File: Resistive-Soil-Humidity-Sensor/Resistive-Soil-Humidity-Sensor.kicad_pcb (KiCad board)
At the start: 2 copper layers, 6 parts, among them Q1 BC547

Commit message: add pcb-layout
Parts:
- added H1: sensor, custom_libraryies:MountingHole.1.8mm, F.Cu at (231.8, 146.3)
- added H2: MountingHole_Pad, custom_libraryies:MountingHole.1.8mm, F.Cu at (231.8, 144.0)
- +9V1: moved to B.Cu
- moved Q1 134.5 mm to (218.8, 149.5)
- moved D1 131.4 mm to (209.7, 147.9), turned to 90 degrees
- moved R1 129.2 mm to (201.3, 144.1)
- moved Voltage-Reg1 127.5 mm to (193.7, 149.2)
- moved +9V1 127.3 mm to (187.1, 149.1)
- moved RV1 119.3 mm to (200.3, 147.6)
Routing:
- net Net-(BZ1-Pad1): track 0.00 -> 45.5 mm
- net Net-(+9V1-Pad2): track 0.00 -> 42.1 mm
- net Net-(H1-Pad1): track 0.00 -> 33.8 mm
- net Net-(BZ1-Pad2): track 0.00 -> 10.2 mm
- net Net-(D1-Pad2): track 0.00 -> 8.49 mm
- net Net-(+9V1-Pad1): track 0.00 -> 6.57 mm

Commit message: update footprints & recover design
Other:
- net class Default removed

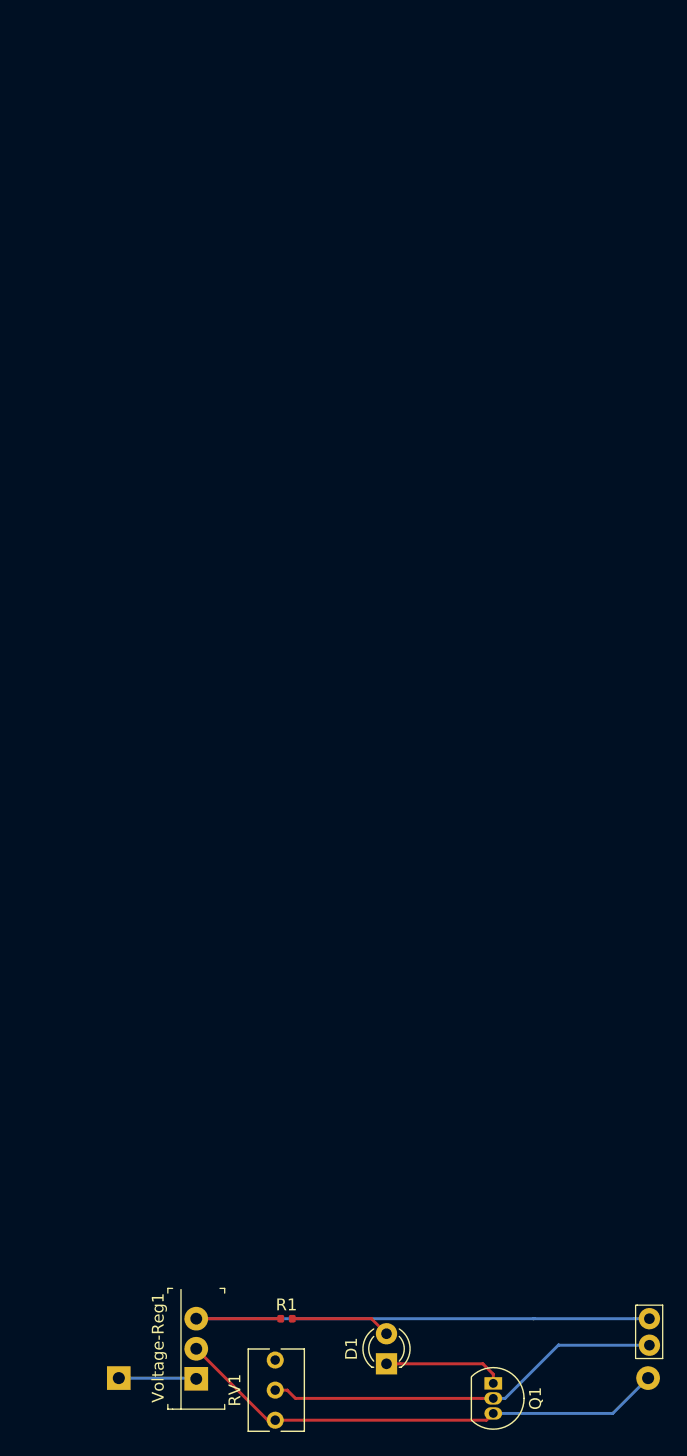
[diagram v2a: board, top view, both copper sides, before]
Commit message: update the design for new power supply
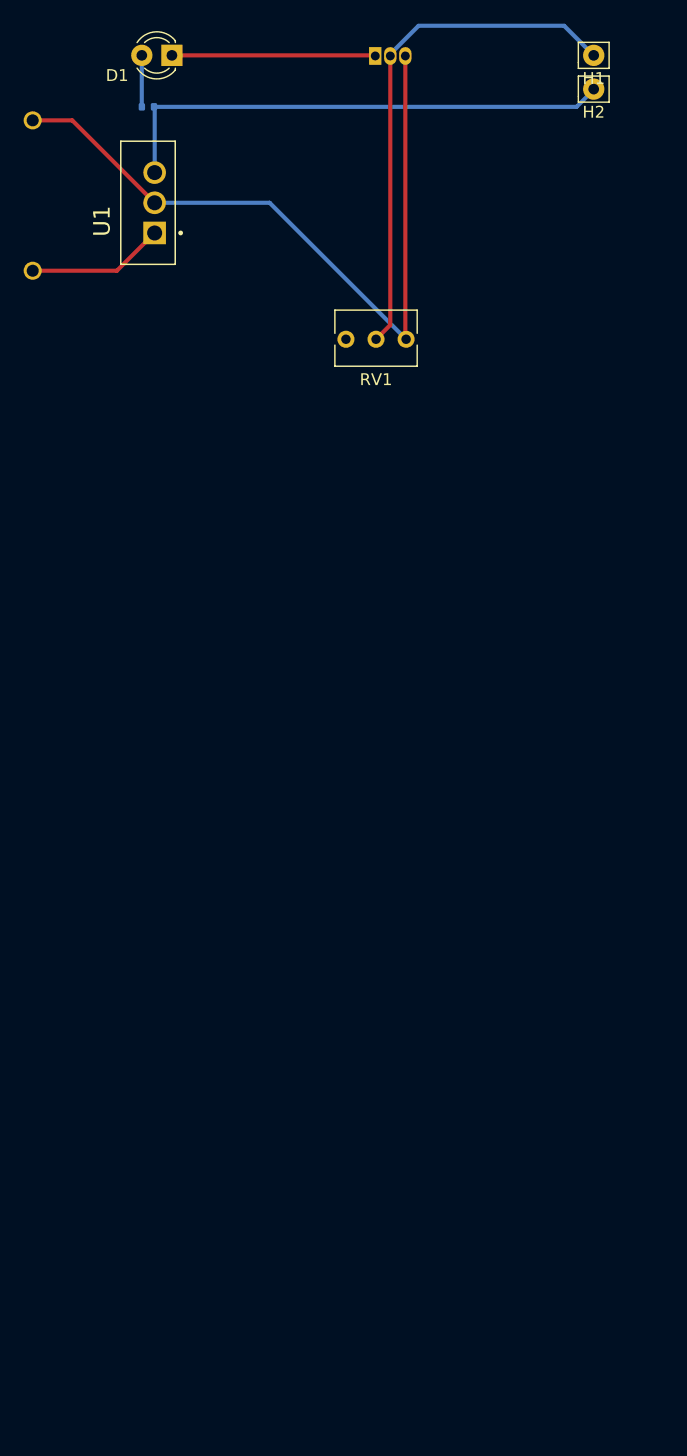
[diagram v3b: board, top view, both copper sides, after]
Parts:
- removed +9V1: Battery, Battery:BatteryHolder_Keystone_2466_1xAAA
- removed Voltage-Reg1: L7805CV, digikey-footprints:TO-220-3
- added 9V1: BH9VPC, BHVPC-BatteryHolder:BAT_BH9VPC, B.Cu at (204.8, 49.2)
- added U1: L7805CV, L7805CV-Vreg:TO255P1040X460X1968-3, F.Cu at (190.2, 52.4)
- H1: value sensor -> MountingHole_Pad; footprint custom_libraryies:MountingHole.1.8mm -> Connector_Pin:Pin_D0.9mm_L10.0mm_W2.4mm_FlatFork
- H2: footprint custom_libraryies:MountingHole.1.8mm -> Connector_Pin:Pin_D0.9mm_L10.0mm_W2.4mm_FlatFork
- Q1, R1: moved to B.Cu
- moved Q1 112.5 mm to (208.8, 37.4), turned to 0 degrees
- moved D1 112.0 mm to (191.6, 37.4), turned to 180 degrees
- moved H1 109.0 mm to (227.2, 37.4), turned to 0 degrees
- moved H2 103.9 mm to (227.2, 40.2), turned to 0 degrees
- moved R1 103.0 mm to (189.6, 41.7), turned to 180 degrees
- moved RV1 86.4 mm to (206.3, 61.4), turned to 180 degrees
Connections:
- RV1 pad 1: Net-(RV1-Pad1) -> unconnected-(RV1-Pad1)
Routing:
- net Net-(9V1-Pad-): track 42.1 -> 63.1 mm
- net Net-(9V1-Pad+): track 0.00 -> 11.6 mm
- net Net-(Q1-Pad2): track 33.8 -> 43.8 mm
- net Net-(BZ1-Pad2): track 10.2 -> 17.2 mm
- net Net-(+9V1-Pad1): track 6.57 -> 0.00 mm
- net Net-(D1-Pad2): track 8.49 -> 4.35 mm
- net Net-(BZ1-Pad1): track 45.5 -> 43.4 mm

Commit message: update the backups
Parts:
- moved H2 139.5 mm to (149.7, 156.2)
- moved R1 139.5 mm to (112.0, 157.7)
- moved RV1 139.5 mm to (128.8, 177.3)
- moved 9V1 139.5 mm to (127.3, 165.2)
- moved D1 139.5 mm to (114.1, 153.3)
- moved H1 139.5 mm to (149.7, 153.3)
- moved Q1 139.5 mm to (131.2, 153.4)
- moved U1 139.5 mm to (112.6, 168.3)
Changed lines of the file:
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@@
   )
   (paper "A4")
+  (title_block
+    (comment 1 "180208063")
+  )
   (layers
     (0 "F.Cu" signal)
@@
   (net 7 "Net-(9V1-Pad+)")
   (footprint "Connector_Pin:Pin_D0.9mm_L10.0mm_W2.4mm_FlatFork" (layer "F.Cu")
-    (at 227.2415 37.3895)
+    (at 149.6915 153.3395)
     (descr "solder Pin_ with flat fork, hole diameter 0.9mm, length 10.0mm, width 2.4mm")
     (tags "solder Pin_ with flat fork")
@@
   )
   (footprint "L7805CV-Vreg:TO255P1040X460X1968-3" (layer "F.Cu")
-    (at 190.1595 52.3895 90)
+    (at 112.6095 168.3395 90)
     (property "MANUFACTURER" "STMicroelectronics")
     (property "PARTREV" "36")
@@
   )
   (footprint "Connector_Pin:Pin_D0.9mm_L10.0mm_W2.4mm_FlatFork" (layer "F.Cu")
-    (at 227.2415 40.2395)
+    (at 149.6915 156.1895)
     (descr "solder Pin_ with flat fork, hole diameter 0.9mm, length 10.0mm, width 2.4mm")
     (tags "solder Pin_ with flat fork")
@@
   )
   (footprint "LED_THT:LED_D3.0mm_FlatTop" (layer "F.Cu")
-    (at 191.6165 37.3895 180)
+    (at 114.0665 153.3395 180)
     (descr "LED, Round, FlatTop, diameter 3.0mm, 2 pins, http://www.kingbright.com/attachments/file/psearch/000/00/00/L-47XEC(Ver.9A).pdf")
     (tags "LED Round FlatTop diameter 3.0mm 2 pins")
@@
   )
   (footprint "Potentiometer_THT:Potentiometer_Bourns_3266Y_Vertical" (layer "F.Cu")
-    (at 206.3165 61.3645 180)
+    (at 128.7665 177.3145 180)
     (descr "Potentiometer, vertical, Bourns 3266Y, https://www.bourns.com/docs/Product-Datasheets/3266.pdf")
     (tags "Potentiometer vertical Bourns 3266Y")
@@
   )
   (footprint "Package_TO_SOT_THT:TO-92_Inline" (layer "B.Cu")
-    (at 208.7915 37.4395)
+    (at 131.2415 153.3895)
     (descr "TO-92 leads in-line, narrow, oval pads, drill 0.75mm (see NXP sot054_po.pdf)")
     (tags "to-92 sc-43 sc-43a sot54 PA33 transistor")
@@
   )
   (footprint "BHVPC-BatteryHolder:BAT_BH9VPC" (layer "B.Cu")
-    (at 204.8065 49.2295 180)
+    (at 127.2565 165.1795 180)
     (property "MANUFACTURER" "MPD")
     (property "MAXIMUM_PACKAGE_HEIGHT" "20.62mm")
@@
   )
   (footprint "Resistor_SMD:R_0402_1005Metric" (layer "B.Cu")
-    (at 189.5915 41.7395 180)
+    (at 112.0415 157.6895 180)
     (descr "Resistor SMD 0402 (1005 Metric), square (rectangular) end terminal, IPC_7351 nominal, (Body size source: IPC-SM-782 page 72, https://www.pcb-3d.com/wordpress/wp-content/uploads/ipc-sm-782a_amendment_1_and_2.pdf), generated with kicad-footprint-generator")
     (tags "resistor")
@@
   )
   (dimension (type aligned) (layer "B.Cu")
-    (pts (xy 177.4915 64.4895) (xy 232.2915 64.5895))
+    (pts (xy 99.9415 180.4395) (xy 154.7415 180.5395))
     (height 4.500904)
-    (gr_text "54,8001 mm" (at 204.886572 67.2404 359.8954458) (layer "B.Cu")
+    (gr_text "54,8001 mm" (at 127.336572 183.1904 359.8954458) (layer "B.Cu")
       (effects (font (size 1.5 1.5) (thickness 0.3)))
     )
@@
   )
   (dimension (type aligned) (layer "B.Cu")
-    (pts (xy 177.3815 33.9795) (xy 177.3815 64.4795))
+    (pts (xy 99.8315 149.9295) (xy 99.8315 180.4295))
     (height 4.44)
-    (gr_text "30,5000 mm" (at 171.1415 49.2295 90) (layer "B.Cu")
+    (gr_text "30,5000 mm" (at 93.5915 165.1795 90) (layer "B.Cu")
       (effects (font (size 1.5 1.5) (thickness 0.3)))
     )
@@
     (style (thickness 0.1) (arrow_length 1.27) (text_position_mode 0) (extension_height 0.58642) (extension_offset 0.5) keep_text_aligned)
   )
-  (segment (start 210.0615 37.4395) (end 210.0615 60.1595) (width 0.35) (layer "F.Cu") (net 2))
-  (segment (start 210.0615 60.1595) (end 208.8565 61.3645) (width 0.35) (layer "F.Cu") (net 2))
-  (segment (start 212.4415 34.8895) (end 224.7415 34.8895) (width 0.35) (layer "B.Cu") (net 2))
-  (segment (start 224.7415 34.8895) (end 227.2415 37.3895) (width 0.35) (layer "B.Cu") (net 2))
-  (segment (start 210.0615 37.282418) (end 212.4415 34.902418) (width 0.35) (layer "B.Cu") (net 2))
-  (segment (start 212.4415 34.902418) (end 212.4415 34.8895) (width 0.25) (layer "B.Cu") (net 2))
-  (segment (start 210.0615 37.4395) (end 210.0615 37.282418) (width 0.25) (layer "B.Cu") (net 2))
-  (segment (start 191.6165 37.3895) (end 208.7415 37.3895) (width 0.35) (layer "F.Cu") (net 3))
-  (segment (start 208.7415 37.3895) (end 208.7915 37.4395) (width 0.25) (layer "F.Cu") (net 3))
-  (segment (start 189.0765 41.7345) (end 189.0765 37.3895) (width 0.35) (layer "B.Cu") (net 4))
-  (segment (start 189.0815 41.7395) (end 189.0765 41.7345) (width 0.25) (layer "B.Cu") (net 4))
-  (segment (start 190.1595 41.7975) (end 190.1015 41.7395) (width 0.25) (layer "B.Cu") (net 5))
-  (segment (start 190.1015 41.7395) (end 225.7915 41.7395) (width 0.35) (layer "B.Cu") (net 5))
-  (segment (start 190.1595 47.2895) (end 190.1595 41.7975) (width 0.35) (layer "B.Cu") (net 5))
-  (segment (start 225.7915 41.7395) (end 227.2915 40.2395) (width 0.35) (layer "B.Cu") (net 5))
-  (segment (start 179.8615 42.8795) (end 183.1995 42.8795) (width 0.35) (layer "F.Cu") (net 6))
-  (segment (start 183.1995 42.8795) (end 190.1595 49.8395) (width 0.35) (layer "F.Cu") (net 6))
-  (segment (start 211.3315 37.4395) (end 211.3315 61.2995) (width 0.35) (layer "F.Cu") (net 6))
-  (segment (start 211.3315 61.2995) (end 211.3965 61.3645) (width 0.25) (layer "F.Cu") (net 6))
-  (segment (start 199.8715 49.8395) (end 211.3965 61.3645) (width 0.35) (layer "B.Cu") (net 6))
-  (segment (start 190.1595 49.8395) (end 199.8715 49.8395) (width 0.35) (layer "B.Cu") (net 6))
-  (segment (start 186.9695 55.5795) (end 190.1595 52.3895) (width 0.35) (layer "F.Cu") (net 7))
-  (segment (start 179.8615 55.5795) (end 186.9695 55.5795) (width 0.35) (layer "F.Cu") (net 7))
+  (segment (start 132.5115 153.3895) (end 132.5115 176.1095) (width 0.35) (layer "F.Cu") (net 2))
+  (segment (start 132.5115 176.1095) (end 131.3065 177.3145) (width 0.35) (layer "F.Cu") (net 2))
+  (segment (start 134.8915 150.8395) (end 147.1915 150.8395) (width 0.35) (layer "B.Cu") (net 2))
+  (segment (start 147.1915 150.8395) (end 149.6915 153.3395) (width 0.35) (layer "B.Cu") (net 2))
+  (segment (start 132.5115 153.232418) (end 134.8915 150.852418) (width 0.35) (layer "B.Cu") (net 2))
+  (segment (start 134.8915 150.852418) (end 134.8915 150.8395) (width 0.25) (layer "B.Cu") (net 2))
+  (segment (start 132.5115 153.3895) (end 132.5115 153.232418) (width 0.25) (layer "B.Cu") (net 2))
+  (segment (start 114.0665 153.3395) (end 131.1915 153.3395) (width 0.35) (layer "F.Cu") (net 3))
+  (segment (start 131.1915 153.3395) (end 131.2415 153.3895) (width 0.25) (layer "F.Cu") (net 3))
+  (segment (start 111.5265 157.6845) (end 111.5265 153.3395) (width 0.35) (layer "B.Cu") (net 4))
+  (segment (start 111.5315 157.6895) (end 111.5265 157.6845) (width 0.25) (layer "B.Cu") (net 4))
+  (segment (start 112.6095 157.7475) (end 112.5515 157.6895) (width 0.25) (layer "B.Cu") (net 5))
+  (segment (start 112.5515 157.6895) (end 148.2415 157.6895) (width 0.35) (layer "B.Cu") (net 5))
+  (segment (start 112.6095 163.2395) (end 112.6095 157.7475) (width 0.35) (layer "B.Cu") (net 5))
+  (segment (start 148.2415 157.6895) (end 149.7415 156.1895) (width 0.35) (layer "B.Cu") (net 5))
+  (segment (start 102.3115 158.8295) (end 105.6495 158.8295) (width 0.35) (layer "F.Cu") (net 6))
+  (segment (start 105.6495 158.8295) (end 112.6095 165.7895) (width 0.35) (layer "F.Cu") (net 6))
+  (segment (start 133.7815 153.3895) (end 133.7815 177.2495) (width 0.35) (layer "F.Cu") (net 6))
+  (segment (start 133.7815 177.2495) (end 133.8465 177.3145) (width 0.25) (layer "F.Cu") (net 6))
+  (segment (start 122.3215 165.7895) (end 133.8465 177.3145) (width 0.35) (layer "B.Cu") (net 6))
+  (segment (start 112.6095 165.7895) (end 122.3215 165.7895) (width 0.35) (layer "B.Cu") (net 6))
+  (segment (start 109.4195 171.5295) (end 112.6095 168.3395) (width 0.35) (layer "F.Cu") (net 7))
+  (segment (start 102.3115 171.5295) (end 109.4195 171.5295) (width 0.35) (layer "F.Cu") (net 7))
 )

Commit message: closing the project
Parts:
- removed the 9V1 at (127.3, 165.2)
- removed the D1 at (114.1, 153.3)
- removed the H1 at (149.7, 153.3)
- removed the H2 at (149.7, 156.2)
- removed the Q1 at (131.2, 153.4)
- removed the R1 at (112.0, 157.7)
- removed the RV1 at (128.8, 177.3)
- removed the U1 at (112.6, 168.3)
- added 9V1: BH9VPC, BHVPC-BatteryHolder:BAT_BH9VPC, B.Cu at (237.0, 73.5)
- added 9V1: BH9VPC, BHVPC-BatteryHolder:BAT_BH9VPC, B.Cu at (237.0, 122.3)
- added 9V1: BH9VPC, BHVPC-BatteryHolder:BAT_BH9VPC, B.Cu at (138.6, 73.3)
- added 9V1: BH9VPC, BHVPC-BatteryHolder:BAT_BH9VPC, B.Cu at (42.8, 30.5)
- added 9V1: BH9VPC, BHVPC-BatteryHolder:BAT_BH9VPC, B.Cu at (138.9, 29.7)
- added 9V1: BH9VPC, BHVPC-BatteryHolder:BAT_BH9VPC, B.Cu at (237.2, 29.9)
- added 9V1: BH9VPC, BHVPC-BatteryHolder:BAT_BH9VPC, B.Cu at (42.6, 122.8)
- added 9V1: BH9VPC, BHVPC-BatteryHolder:BAT_BH9VPC, B.Cu at (138.6, 122.0)
- added 9V1: BH9VPC, BHVPC-BatteryHolder:BAT_BH9VPC, B.Cu at (42.6, 74.1)
- added D1: LED, LED_THT:LED_D3.0mm_FlatTop, F.Cu at (125.4, 61.4)
- added D1: LED, LED_THT:LED_D3.0mm_FlatTop, F.Cu at (224.0, 18.1)
- added D1: LED, LED_THT:LED_D3.0mm_FlatTop, F.Cu at (29.4, 111.0)
- added D1: LED, LED_THT:LED_D3.0mm_FlatTop, F.Cu at (125.7, 17.8)
- added D1: LED, LED_THT:LED_D3.0mm_FlatTop, F.Cu at (29.6, 18.7)
- added D1: LED, LED_THT:LED_D3.0mm_FlatTop, F.Cu at (125.4, 110.2)
- added D1: LED, LED_THT:LED_D3.0mm_FlatTop, F.Cu at (223.8, 110.5)
- added D1: LED, LED_THT:LED_D3.0mm_FlatTop, F.Cu at (223.8, 61.7)
- added D1: LED, LED_THT:LED_D3.0mm_FlatTop, F.Cu at (29.4, 62.2)
- added H1: MountingHole_Pad, Connector_Pin:Pin_D0.9mm_L10.0mm_W2.4mm_FlatFork, F.Cu at (161.1, 61.4)
- added H1: MountingHole_Pad, Connector_Pin:Pin_D0.9mm_L10.0mm_W2.4mm_FlatFork, F.Cu at (65.3, 18.7)
- added H1: MountingHole_Pad, Connector_Pin:Pin_D0.9mm_L10.0mm_W2.4mm_FlatFork, F.Cu at (65.0, 111.0)
- added H1: MountingHole_Pad, Connector_Pin:Pin_D0.9mm_L10.0mm_W2.4mm_FlatFork, F.Cu at (259.7, 18.1)
- added H1: MountingHole_Pad, Connector_Pin:Pin_D0.9mm_L10.0mm_W2.4mm_FlatFork, F.Cu at (161.1, 110.2)
- added H1: MountingHole_Pad, Connector_Pin:Pin_D0.9mm_L10.0mm_W2.4mm_FlatFork, F.Cu at (161.3, 17.8)
- added H1: MountingHole_Pad, Connector_Pin:Pin_D0.9mm_L10.0mm_W2.4mm_FlatFork, F.Cu at (259.4, 110.5)
- added H1: MountingHole_Pad, Connector_Pin:Pin_D0.9mm_L10.0mm_W2.4mm_FlatFork, F.Cu at (259.4, 61.7)
- added H1: MountingHole_Pad, Connector_Pin:Pin_D0.9mm_L10.0mm_W2.4mm_FlatFork, F.Cu at (65.0, 62.2)
- added H2: MountingHole_Pad, Connector_Pin:Pin_D0.9mm_L10.0mm_W2.4mm_FlatFork, F.Cu at (259.7, 21.0)
- added H2: MountingHole_Pad, Connector_Pin:Pin_D0.9mm_L10.0mm_W2.4mm_FlatFork, F.Cu at (161.3, 20.7)
- added H2: MountingHole_Pad, Connector_Pin:Pin_D0.9mm_L10.0mm_W2.4mm_FlatFork, F.Cu at (259.4, 64.5)
- added H2: MountingHole_Pad, Connector_Pin:Pin_D0.9mm_L10.0mm_W2.4mm_FlatFork, F.Cu at (65.0, 65.1)
- added H2: MountingHole_Pad, Connector_Pin:Pin_D0.9mm_L10.0mm_W2.4mm_FlatFork, F.Cu at (65.0, 113.9)
- added H2: MountingHole_Pad, Connector_Pin:Pin_D0.9mm_L10.0mm_W2.4mm_FlatFork, F.Cu at (161.1, 113.0)
- added H2: MountingHole_Pad, Connector_Pin:Pin_D0.9mm_L10.0mm_W2.4mm_FlatFork, F.Cu at (161.1, 64.3)
- added H2: MountingHole_Pad, Connector_Pin:Pin_D0.9mm_L10.0mm_W2.4mm_FlatFork, F.Cu at (65.3, 21.5)
- added H2: MountingHole_Pad, Connector_Pin:Pin_D0.9mm_L10.0mm_W2.4mm_FlatFork, F.Cu at (259.4, 113.3)
- added Q1: BC547, Package_TO_SOT_THT:TO-92_Inline, B.Cu at (46.6, 62.3)
- added Q1: BC547, Package_TO_SOT_THT:TO-92_Inline, B.Cu at (241.0, 61.7)
- added Q1: BC547, Package_TO_SOT_THT:TO-92_Inline, B.Cu at (142.6, 110.2)
- added Q1: BC547, Package_TO_SOT_THT:TO-92_Inline, B.Cu at (241.0, 110.5)
- added Q1: BC547, Package_TO_SOT_THT:TO-92_Inline, B.Cu at (46.6, 111.1)
- added Q1: BC547, Package_TO_SOT_THT:TO-92_Inline, B.Cu at (46.8, 18.7)
- added Q1: BC547, Package_TO_SOT_THT:TO-92_Inline, B.Cu at (142.6, 61.5)
- added Q1: BC547, Package_TO_SOT_THT:TO-92_Inline, B.Cu at (241.2, 18.2)
- added Q1: BC547, Package_TO_SOT_THT:TO-92_Inline, B.Cu at (142.9, 17.9)
- added R1: 1kohm, Resistor_SMD:R_0402_1005Metric, B.Cu at (222.0, 22.5)
- added R1: 1kohm, Resistor_SMD:R_0402_1005Metric, B.Cu at (123.4, 65.8)
- added R1: 1kohm, Resistor_SMD:R_0402_1005Metric, B.Cu at (27.4, 115.4)
- added R1: 1kohm, Resistor_SMD:R_0402_1005Metric, B.Cu at (27.4, 66.6)
- added R1: 1kohm, Resistor_SMD:R_0402_1005Metric, B.Cu at (221.8, 114.8)
- added R1: 1kohm, Resistor_SMD:R_0402_1005Metric, B.Cu at (123.7, 22.2)
- added R1: 1kohm, Resistor_SMD:R_0402_1005Metric, B.Cu at (221.8, 66.0)
- added R1: 1kohm, Resistor_SMD:R_0402_1005Metric, B.Cu at (123.4, 114.5)
- added R1: 1kohm, Resistor_SMD:R_0402_1005Metric, B.Cu at (27.6, 23.0)
- added RV1: R_POT, Potentiometer_THT:Potentiometer_Bourns_3266Y_Vertical, F.Cu at (140.1, 134.2)
- added RV1: R_POT, Potentiometer_THT:Potentiometer_Bourns_3266Y_Vertical, F.Cu at (140.1, 85.4)
- added RV1: R_POT, Potentiometer_THT:Potentiometer_Bourns_3266Y_Vertical, F.Cu at (238.4, 85.7)
- added RV1: R_POT, Potentiometer_THT:Potentiometer_Bourns_3266Y_Vertical, F.Cu at (140.3, 41.8)
- added RV1: R_POT, Potentiometer_THT:Potentiometer_Bourns_3266Y_Vertical, F.Cu at (238.4, 134.4)
- added RV1: R_POT, Potentiometer_THT:Potentiometer_Bourns_3266Y_Vertical, F.Cu at (238.7, 42.1)
- added RV1: R_POT, Potentiometer_THT:Potentiometer_Bourns_3266Y_Vertical, F.Cu at (44.3, 42.6)
- added RV1: R_POT, Potentiometer_THT:Potentiometer_Bourns_3266Y_Vertical, F.Cu at (44.0, 135.0)
- added RV1: R_POT, Potentiometer_THT:Potentiometer_Bourns_3266Y_Vertical, F.Cu at (44.0, 86.2)
- added U1: L7805CV, L7805CV-Vreg:TO255P1040X460X1968-3, F.Cu at (222.3, 76.7)
- added U1: L7805CV, L7805CV-Vreg:TO255P1040X460X1968-3, F.Cu at (27.9, 77.2)
- added U1: L7805CV, L7805CV-Vreg:TO255P1040X460X1968-3, F.Cu at (27.9, 126.0)
- added U1: L7805CV, L7805CV-Vreg:TO255P1040X460X1968-3, F.Cu at (124.0, 76.4)
- added U1: L7805CV, L7805CV-Vreg:TO255P1040X460X1968-3, F.Cu at (28.2, 33.7)
- added U1: L7805CV, L7805CV-Vreg:TO255P1040X460X1968-3, F.Cu at (124.0, 125.2)
- added U1: L7805CV, L7805CV-Vreg:TO255P1040X460X1968-3, F.Cu at (222.6, 33.1)
- added U1: L7805CV, L7805CV-Vreg:TO255P1040X460X1968-3, F.Cu at (222.3, 125.5)
- added U1: L7805CV, L7805CV-Vreg:TO255P1040X460X1968-3, F.Cu at (124.2, 32.8)
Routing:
- net Net-(9V1-Pad-): track 63.1 -> 850.1 mm
- net Net-(Q1-Pad2): track 43.8 -> 401.0 mm
- net Net-(BZ1-Pad1): track 43.4 -> 382.8 mm
- net Net-(BZ1-Pad2): track 17.2 -> 154.8 mm
- net Net-(9V1-Pad+): track 11.6 -> 104.6 mm
- net Net-(D1-Pad2): track 4.35 -> 49.1 mm
